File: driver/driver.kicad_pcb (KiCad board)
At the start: 2 copper layers, 100 x 62 mm, 60 parts, among them J1 ED550/4DS, J2 PJ-051AH, J3 TC2050, K1 J107F1AS125VDC, Q1 AOSS32334C, Q2 AOSS32334C, SW1 B3S-1000, SW2 B3S-1000, SW3 B3S-1000, U1 OPA4196IDR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

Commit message: Added data matrix codes to PCBs for easy identification
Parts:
- added G***: LOGO, LOGO, B.Cu at (238.4, 63.1)
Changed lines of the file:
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@@
+		)
+	)
+	(footprint "LOGO"
+		(layer "B.Cu")
+		(at 238.4 63.1 180)
+		(property "Reference" "G***"
+			(at 0 0 0)
+			(layer "B.SilkS")
+			(hide yes)
+			(effects
+				(font
+					(size 1.5 1.5)
+					(thickness 0.3)
+				)
+				(justify mirror)
+			)
+		)
+		(property "Value" "LOGO"
+			(at 0.75 0 0)
+			(layer "B.SilkS")
+			(hide yes)
+			(effects
+				(font
+					(size 1.5 1.5)
+					(thickness 0.3)
+				)
+				(justify mirror)
+			)
+		)
+		(property "Footprint" ""
+			(at 0 0 0)
+			(layer "B.Fab")
+			(hide yes)
+			(effects
+				(font
+					(size 1.27 1.27)
+					(thickness 0.15)
+				)
+				(justify mirror)
+			)
+		)
+		(property "Datasheet" ""
+			(at 0 0 0)
+			(layer "B.Fab")
+			(hide yes)
+			(effects
+				(font
+					(size 1.27 1.27)
+					(thickness 0.15)
+				)
+				(justify mirror)
+			)
+		)
+		(property "Description" ""
+			(at 0 0 0)
+			(layer "B.Fab")
+			(hide yes)
+			(effects
+				(font
+					(size 1.27 1.27)
+					(thickness 0.15)
+				)
+				(justify mirror)
+			)
+		)
+		(attr board_only exclude_from_pos_files exclude_from_bom)
+		(fp_poly
+			(pts
+				(xy -2.883994 -2.536526) (xy -2.883994 -2.883995) (xy -2.171682 -2.883995) (xy -1.45937 -2.883995)
+				(xy -1.45937 -3.248837) (xy -1.45937 -3.61368) (xy -2.536525 -3.61368) (xy -3.61368 -3.61368) (xy -3.61368 -2.901368)
+				(xy -3.61368 -2.189056) (xy -3.248837 -2.189056) (xy -2.883994 -2.189056)
+			)
+			(stroke
+				(width 0)
+				(type solid)
+			)
+			(fill solid)
+			(layer "B.SilkS")
+		)
+		(fp_poly
+			(pts
+				(xy 5.003557 0) (xy 5.003557 -5.003557) (xy 0 -5.003557) (xy -5.003556 -5.003557) (xy -5.003556 0)
+				(xy -4.343365 0) (xy -4.343365 -4.343366) (xy 0 -4.343366) (xy 4.343366 -4.343366) (xy 4.343366 -3.978523)
+				(xy 4.343366 -3.61368) (xy 3.978523 -3.61368) (xy 3.61368 -3.61368) (xy 3.61368 -3.248837) (xy 3.61368 -2.883995)
+				(xy 3.978523 -2.883995) (xy 4.343366 -2.883995) (xy 4.343366 -2.536526) (xy 4.343366 -2.189056)
+				(xy 3.978523 -2.189056) (xy 3.61368 -2.189056) (xy 3.61368 -2.536526) (xy 3.61368 -2.883995) (xy 3.248837 -2.883995)
+				(xy 2.883995 -2.883995) (xy 2.883995 -2.171683) (xy 2.883995 -1.459371) (xy 3.61368 -1.459371) (xy 4.343366 -1.459371)
+				(xy 4.343366 -1.094528) (xy 4.343366 -0.729686) (xy 3.266211 -0.729686) (xy 2.189056 -0.729686)
+				(xy 2.189056 -1.80684) (xy 2.189056 -2.883995) (xy 2.536526 -2.883995) (xy 2.883995 -2.883995) (xy 2.883995 -3.248837)
+				(xy 2.883995 -3.61368) (xy 2.171683 -3.61368) (xy 1.459371 -3.61368) (xy 1.459371 -2.536526) (xy 1.459371 -1.459371)
+				(xy 1.094528 -1.459371) (xy 0.729686 -1.459371) (xy 0.729686 -1.094528) (xy 0.729686 -0.729686)
+				(xy 0.364843 -0.729686) (xy 0 -0.729686) (xy 0 -1.459371) (xy 0 -2.189056) (xy 0.364843 -2.189056)
+				(xy 0.729686 -2.189056) (xy 0.729686 -2.901368) (xy 0.729686 -3.61368) (xy 0 -3.61368) (xy -0.729685 -3.61368)
+				(xy -0.729685 -2.901368) (xy -0.729685 -2.189056) (xy -1.80684 -2.189056) (xy -2.883994 -2.189056)
+				(xy -2.883994 -1.094528) (xy -2.883994 0) (xy -2.536525 0) (xy -2.189056 0) (xy -2.189056 -0.729686)
+				(xy -2.189056 -1.459371) (xy -1.824213 -1.459371) (xy -1.45937 -1.459371) (xy -1.45937 -1.094528)
+				(xy -1.45937 -0.729686) (xy -1.094528 -0.729686) (xy -0.729685 -0.729686) (xy -0.729685 0) (xy -0.729685 0.364842)
+				(xy 0 0.364842) (xy 0 0) (xy 0.364843 0) (xy 0.729686 0) (xy 0.729686 0.364842) (xy 0.729686 0.729685)
+				(xy 1.459371 0.729685) (xy 1.459371 -0.729686) (xy 1.824214 -0.729686) (xy 2.189056 -0.729686) (xy 2.189056 0.364842)
+				(xy 3.61368 0.364842) (xy 3.61368 0) (xy 3.978523 0) (xy 4.343366 0) (xy 4.343366 0.364842) (xy 4.343366 0.729685)
+				(xy 3.978523 0.729685) (xy 3.61368 0.729685) (xy 3.61368 0.364842) (xy 2.189056 0.364842) (xy 2.189056 0.729685)
+				(xy 2.189056 1.45937) (xy 2.883995 1.45937) (xy 2.883995 1.094528) (xy 2.883995 0.729685) (xy 3.248837 0.729685)
+				(xy 3.61368 0.729685) (xy 3.61368 1.094528) (xy 3.61368 1.45937) (xy 3.978523 1.45937) (xy 4.343366 1.45937)
+				(xy 4.343366 1.824213) (xy 4.343366 2.189056) (xy 3.978523 2.189056) (xy 3.61368 2.189056) (xy 3.61368 1.824213)
+				(xy 3.61368 1.45937) (xy 3.248837 1.45937) (xy 2.883995 1.45937) (xy 2.189056 1.45937) (xy 2.189056 2.189056)
+				(xy 1.824214 2.189056) (xy 1.459371 2.189056) (xy 1.459371 0.729685) (xy 0.729686 0.729685) (xy 0.364843 0.729685)
+				(xy 0 0.729685) (xy 0 0.364842) (xy -0.729685 0.364842) (xy -0.729685 0.729685) (xy -0.364842 0.729685)
+				(xy 0 0.729685) (xy 0 1.45937) (xy 0 2.189056) (xy -0.729685 2.189056) (xy -1.45937 2.189056) (xy -1.45937 1.824213)
+				(xy -1.45937 1.45937) (xy -1.094528 1.45937) (xy -0.729685 1.45937) (xy -0.729685 1.094528) (xy -0.729685 0.729685)
+				(xy -2.171682 0.729685) (xy -3.61368 0.729685) (xy -3.61368 1.094528) (xy -3.61368 1.45937) (xy -3.248837 1.45937)
+				(xy -2.883994 1.45937) (xy -2.883994 1.824213) (xy -2.883994 2.189056) (xy -3.248837 2.189056) (xy -3.61368 2.189056)
+				(xy -3.61368 2.536525) (xy 0.729686 2.536525) (xy 0.729686 2.189056) (xy 1.094528 2.189056) (xy 1.459371 2.189056)
+				(xy 1.459371 2.536525) (xy 1.459371 2.883994) (xy 1.094528 2.883994) (xy 0.729686 2.883994) (xy 0.729686 2.536525)
+				(xy -3.61368 2.536525) (xy -3.61368 3.26621) (xy -3.61368 3.61368) (xy -2.883994 3.61368) (xy -2.883994 2.883994)
+				(xy -2.536525 2.883994) (xy -2.189056 2.883994) (xy -2.189056 3.61368) (xy -1.45937 3.61368) (xy -1.45937 2.883994)
+				(xy -0.729685 2.883994) (xy 0 2.883994) (xy 0 3.248837) (xy 0 3.26621) (xy 2.883995 3.26621) (xy 2.883995 2.189056)
+				(xy 3.248837 2.189056) (xy 3.61368 2.189056) (xy 3.61368 2.536525) (xy 3.61368 2.883994) (xy 3.978523 2.883994)
+				(xy 4.343366 2.883994) (xy 4.343366 3.248837) (xy 4.343366 3.61368) (xy 3.978523 3.61368) (xy 3.61368 3.61368)
+				(xy 3.61368 3.978522) (xy 3.61368 4.343365) (xy 3.248837 4.343365) (xy 2.883995 4.343365) (xy 2.883995 3.26621)
+				(xy 0 3.26621) (xy 0 3.61368) (xy 0.364843 3.61368) (xy 0.729686 3.61368) (xy 0.729686 3.978522)
+				(xy 1.459371 3.978522) (xy 1.459371 3.61368) (xy 1.824214 3.61368) (xy 2.189056 3.61368) (xy 2.189056 3.978522)
+				(xy 2.189056 4.343365) (xy 1.824214 4.343365) (xy 1.459371 4.343365) (xy 1.459371 3.978522) (xy 0.729686 3.978522)
+				(xy 0.729686 4.343365) (xy 0.364843 4.343365) (xy 0 4.343365) (xy 0 3.978522) (xy 0 3.61368) (xy -0.364842 3.61368)
+				(xy -0.729685 3.61368) (xy -0.729685 3.978522) (xy -0.729685 4.343365) (xy -1.094528 4.343365) (xy -1.45937 4.343365)
+				(xy -1.45937 3.61368) (xy -2.189056 3.61368) (xy -2.189056 4.343365) (xy -2.536525 4.343365) (xy -2.883994 4.343365)
+				(xy -2.883994 3.61368) (xy -3.61368 3.61368) (xy -3.61368 4.343365) (xy -3.978522 4.343365) (xy -4.343365 4.343365)
+				(xy -4.343365 0) (xy -5.003556 0) (xy -5.003556 5.003556) (xy 0 5.003556) (xy 5.003557 5.003556)
+			)
+			(stroke
+				(width 0)
+				(type solid)
+			)
+			(fill solid)
+			(layer "B.SilkS")
 		)
 	)

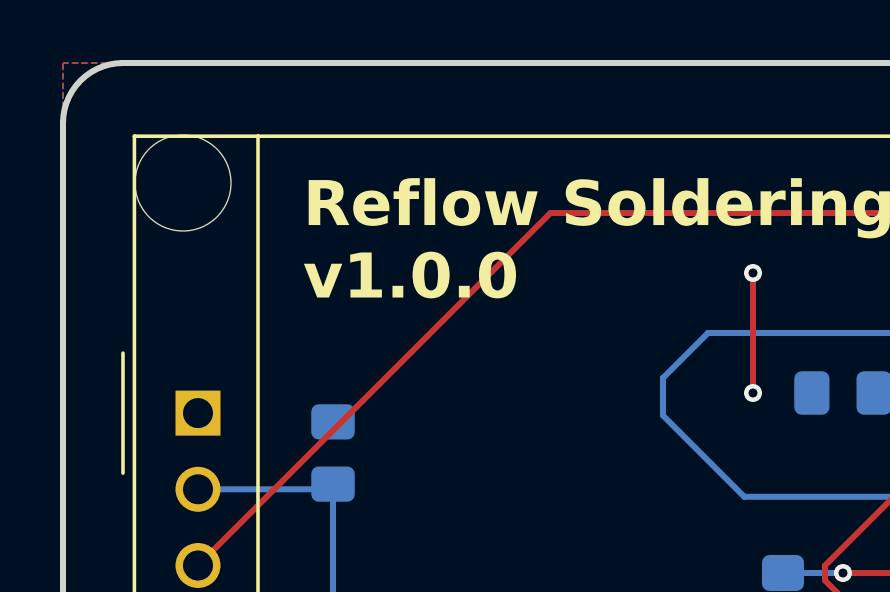
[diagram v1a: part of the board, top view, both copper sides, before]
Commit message: Replaced 5V regulator with fully compatible alternative
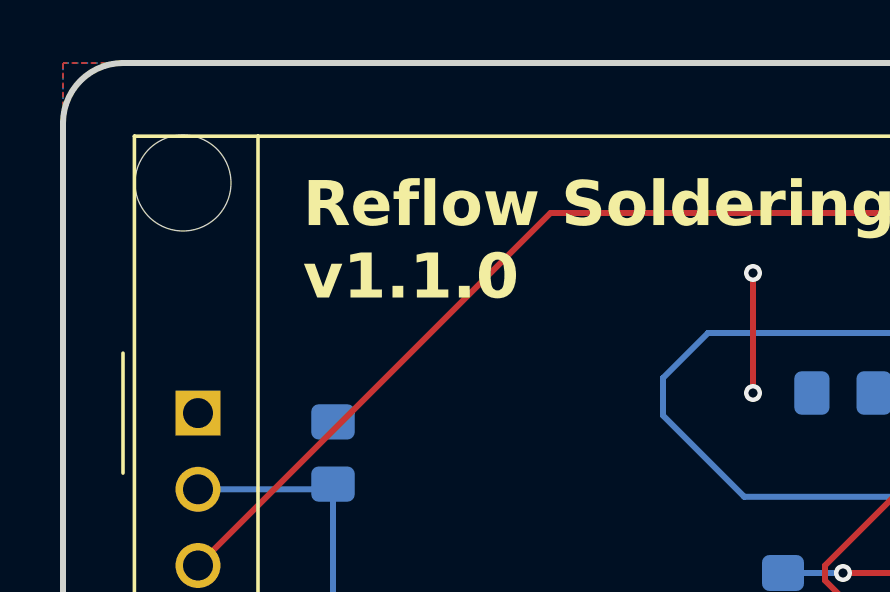
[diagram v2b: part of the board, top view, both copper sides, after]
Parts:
- U2: value LT323AT#PBF -> L7805CV
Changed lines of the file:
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@@
 		(title "Reflow Soldering Hot Plate Driver")
 		(date "2024-070-30")
-		(rev "v1.0.0")
+		(rev "v1.1.0")
 	)
 	(layers
@@
 			)
 		)
-		(property "Value" "LT323AT#PBF"
+		(property "Value" "L7805CV"
 			(at 2.54 -2 180)
 			(layer "B.Fab")
